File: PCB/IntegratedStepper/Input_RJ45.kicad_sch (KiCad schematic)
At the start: 6 parts, among them J1 8P8C, J2 8P8C, J5 Conn_01x05_Socket

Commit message: init PCB dev area
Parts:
- removed J1, J2: 8P8C, easyeda2kicad:RJ45-TH_KH-RJ45-58-8P8C, symbol Connector:8P8C
- added Audio1, Audio2: PJ-327C-4A, easyeda2kicad:AUDIO-SMD_PJ-327C-4A, symbol easyeda2kicad:PJ-327C-4A
- added J6, J7: XT30PW-F, Connector_AMASS:AMASS_XT30PW-F_1x02_P2.50mm_Horizontal, symbol SamacSys_Parts:XT30PW-F
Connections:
- net CANH: now also Audio1.1, Audio2.1
- net CANL: now also Audio1.2, Audio2.2
- net GND: now also J6.1, J7.1
- net VM: now also J6.2, J7.2

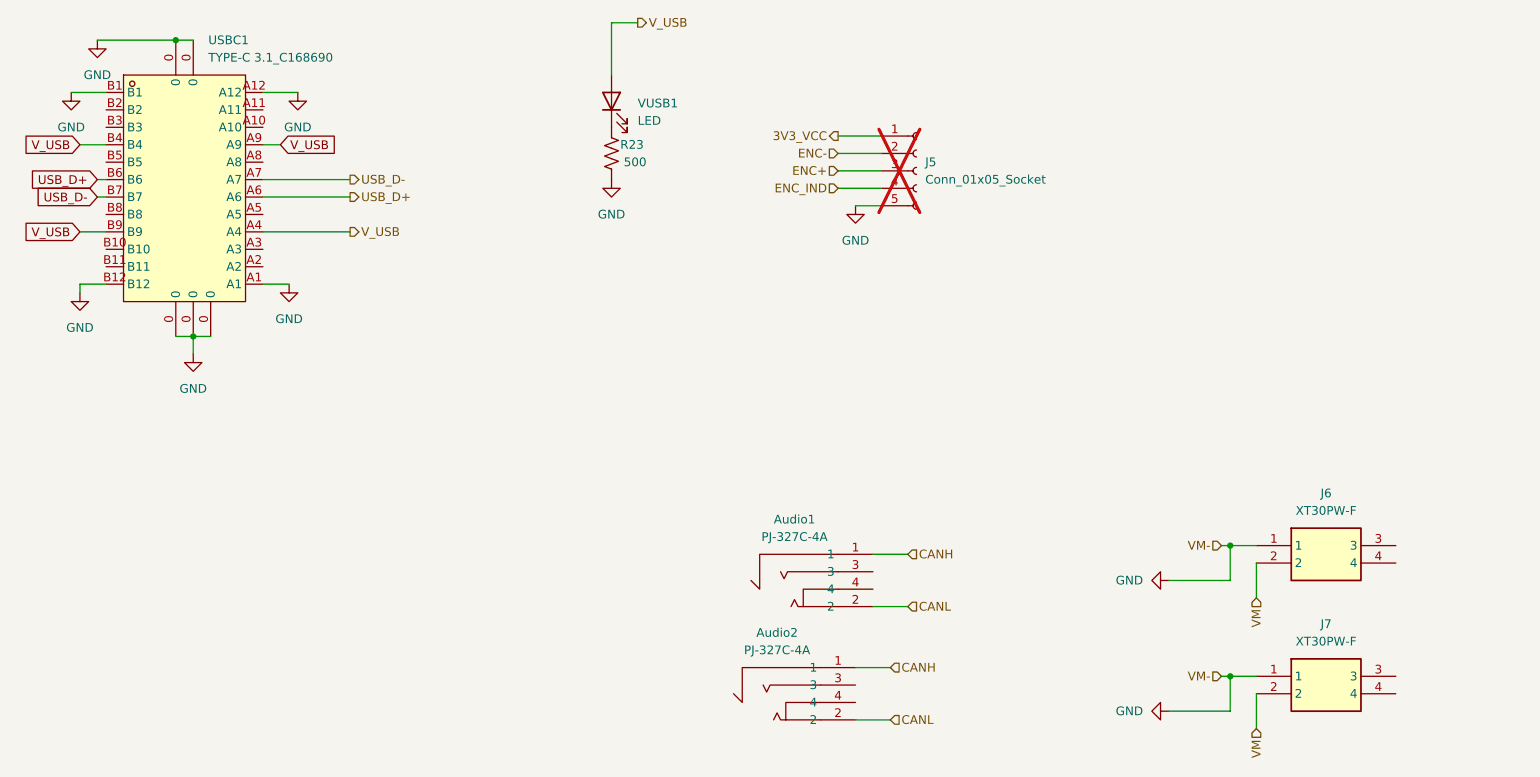
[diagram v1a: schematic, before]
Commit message: Update PCB with DRV8243 for 12A capacity
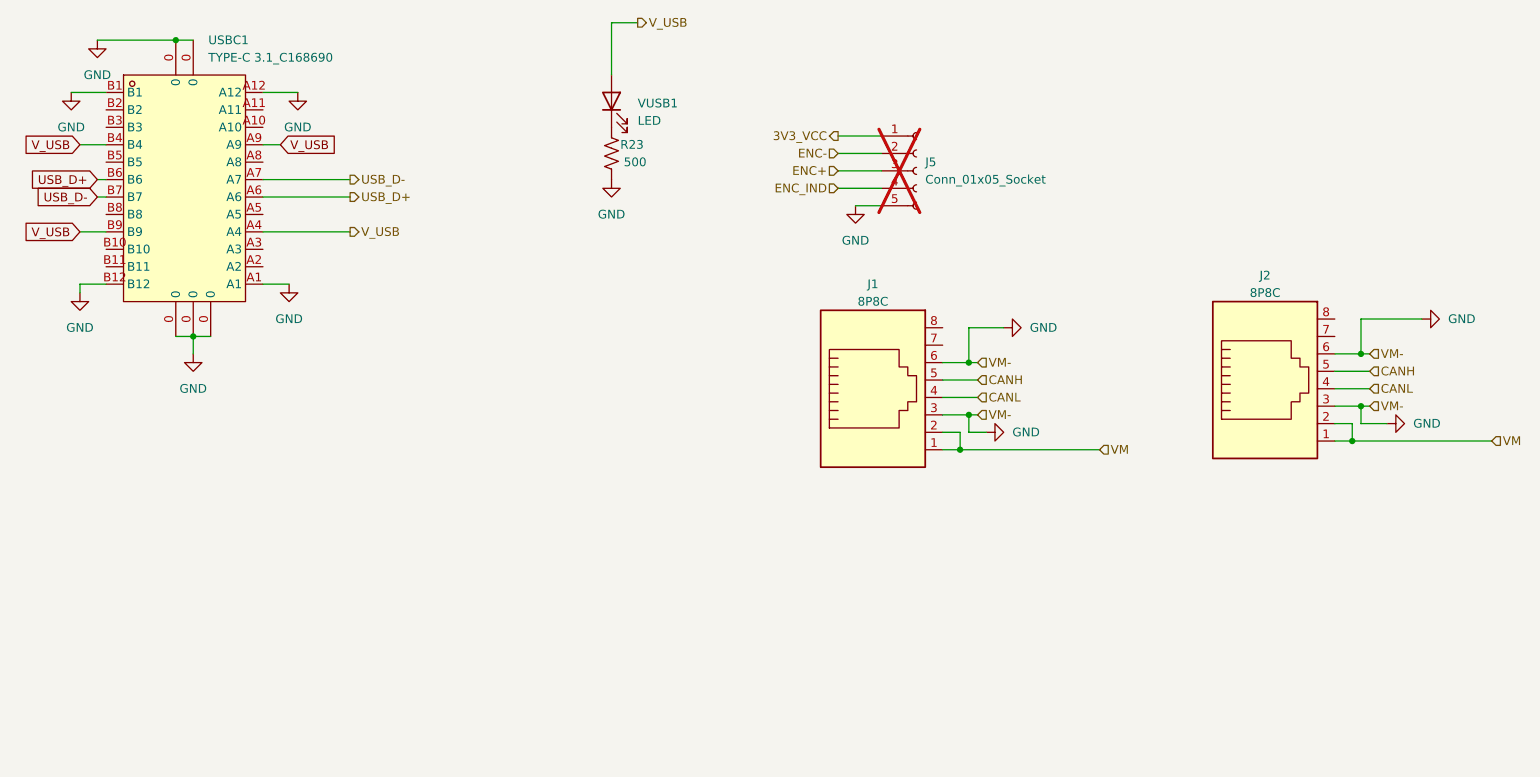
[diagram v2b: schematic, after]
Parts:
- removed Audio1, Audio2: PJ-327C-4A, easyeda2kicad:AUDIO-SMD_PJ-327C-4A, symbol easyeda2kicad:PJ-327C-4A
- removed J6, J7: XT30PW-F, Connector_AMASS:AMASS_XT30PW-F_1x02_P2.50mm_Horizontal, symbol SamacSys_Parts:XT30PW-F
- added J1, J2: 8P8C, easyeda2kicad:RJ45-TH_KH-RJ45-58-8P8C, symbol Connector:8P8C
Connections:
- net CANH: now also J1.5, J2.5
- net CANL: now also J1.4, J2.4
- net GND: now also J1.3, J1.6, J2.3, J2.6
- net VM: now also J1.1, J1.2, J2.1, J2.2

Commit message: update layout temp
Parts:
- removed USBC1: TYPE-C 3.1_C168690, easyeda2kicad:USB-C-SMD_TYPE-C-USB-3, symbol easyeda2kicad:TYPE-C3.1_C168690
- added USB1: GT-USB-7038C, easyeda2kicad:USB-C-TH_G-SWITCH_GT-USB-7038X, symbol easyeda2kicad:GT-USB-7038C
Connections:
- net GND: now also USB1.13 (SHELL), USB1.A1 (GND), USB1.A12 (GND)
- net USB_D+: now also USB1.A6 (Dp1), USB1.B6 (Dp2)
- net USB_D-: now also USB1.A7 (Dn1), USB1.B7 (Dn2)
- net V_USB: now also USB1.A4 (VBUS), USB1.A9 (VBUS)

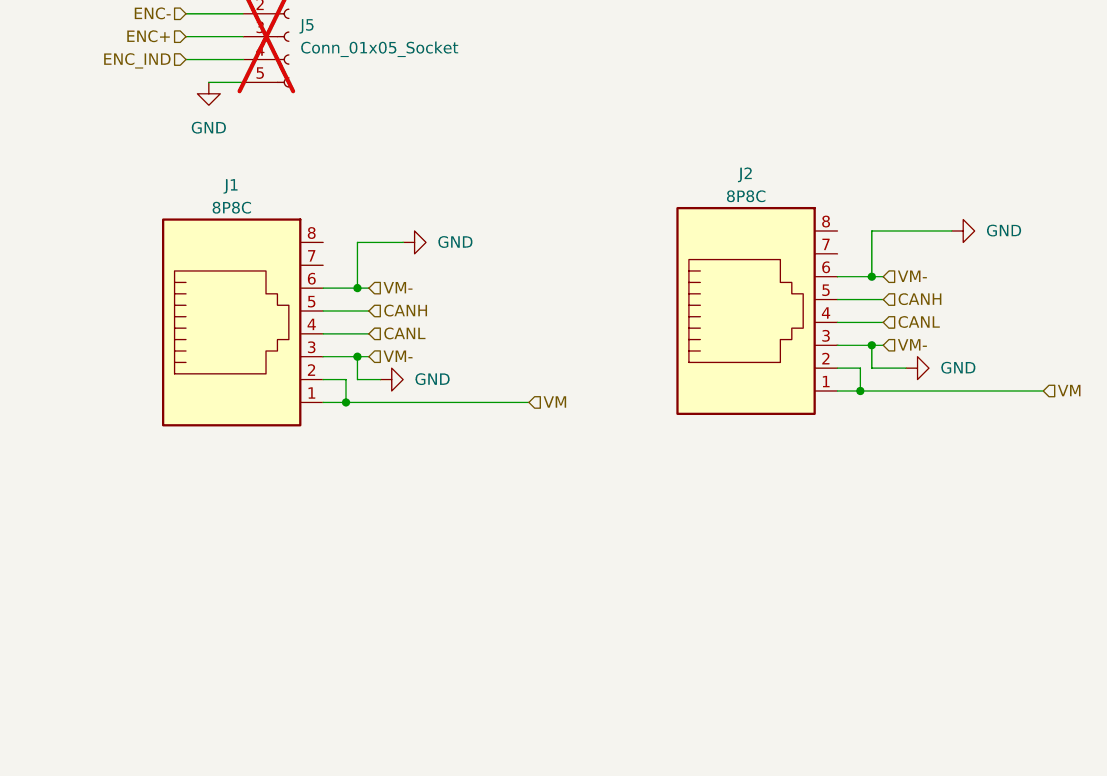
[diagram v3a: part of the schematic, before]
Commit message: update layout to XT30 + 3.5mm Jack
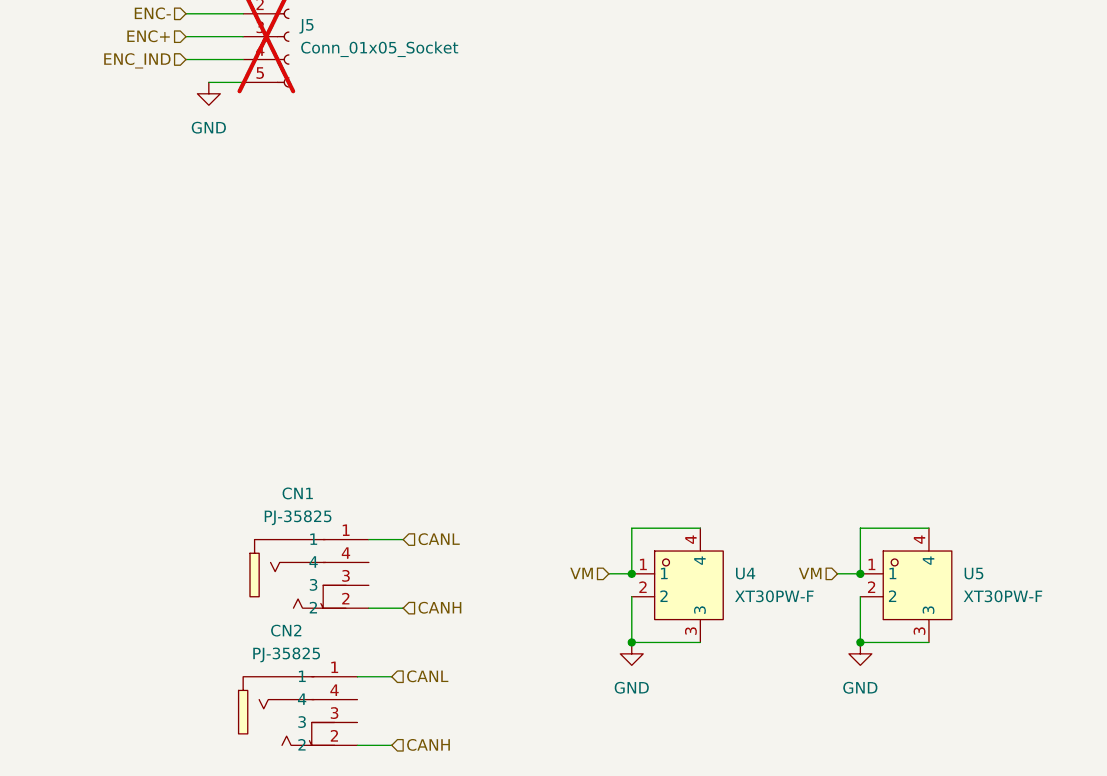
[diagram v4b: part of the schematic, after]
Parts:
- removed J1, J2: 8P8C, easyeda2kicad:RJ45-TH_KH-RJ45-58-8P8C, symbol Connector:8P8C
- added CN1, CN2: PJ-35825, easyeda2kicad:AUDIO-SMD_PJ-35825, symbol easyeda2kicad:PJ-35825
- added U4, U5: XT30PW-F, easyeda2kicad:CONN-TH_XT30PW-F-1, symbol easyeda2kicad:XT30PW-F
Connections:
- net CANH: now also CN1.2, CN2.2
- net CANL: now also CN1.1, CN2.1
- net GND: now also U4.2, U4.3, U5.2, U5.3
- net VM: now also U4.1, U4.4, U5.1, U5.4
